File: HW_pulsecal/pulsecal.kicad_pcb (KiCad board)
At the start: 2 copper layers, 98 x 98 mm, 92 parts, among them J1 BNC_CONN, J2 USB_C_Receptacle_USB2.0, J3 Conn_01x02, J4 Conn_01x04, Q1 AO3401A, Q3 FDG6301N, SW1 SW_Push, SW2 SW_Push, SW3 SW_Push, SW4 SW_Push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

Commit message: update
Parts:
- added REF**: KiCad-Logo2_5mm_SilkScreen, Symbol:KiCad-Logo2_5mm_SilkScreen, F.Cu at (46.2, 99.7)
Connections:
- U5 pad 20: unconnected-(U5-PB1-Pad20) -> DISP_F
- U5 pad 21: unconnected-(U5-PB2-Pad21) -> DISP_D
- U5 pad 22: unconnected-(U5-PB10-Pad22) -> DISP_DIG2
- U5 pad 23: unconnected-(U5-PB11-Pad23) -> DISP_C
- U5 pad 24: unconnected-(U5-PB12-Pad24) -> DISP_J
- U5 pad 26: unconnected-(U5-PB14-Pad26) -> DISP_H
- U5 pad 27: unconnected-(U5-PB15-Pad27) -> DISP_DIG1
- U5 pad 29: unconnected-(U5-PA9/NC-Pad29) -> DISP_DP
- U5 pad 30: unconnected-(U5-PC6-Pad30) -> DISP_A
- U5 pad 31: unconnected-(U5-PC7-Pad31) -> DISP_E
- U5 pad 32: unconnected-(U5-PA10/NC-Pad32) -> DISP_DIG3
- U5 pad 33: unconnected-(U5-PA11/PA9-Pad33) -> DISP_N
- U5 pad 34: unconnected-(U5-PA12/PA10-Pad34) -> DISP_B
- U5 pad 37: unconnected-(U5-PA15-Pad37) -> DISP_M
- U5 pad 38: unconnected-(U5-PD0-Pad38) -> DISP_DIG4
- U5 pad 39: unconnected-(U5-PD1-Pad39) -> DISP_L
- U5 pad 40: unconnected-(U5-PD2-Pad40) -> DISP_DIG5
- U5 pad 41: unconnected-(U5-PD3-Pad41) -> DISP_G2
- U5 pad 42: unconnected-(U5-PB3-Pad42) -> DISP_K
- U5 pad 43: unconnected-(U5-PB4-Pad43) -> DISP_G1
- U5 pad 44: unconnected-(U5-PB5-Pad44) -> DISP_DIG6
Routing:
- net DISP_D: track 0.00 -> 28.2 mm, vias 0 -> 2
- net DISP_F: track 0.00 -> 28.2 mm, vias 0 -> 2
- net DISP_DIG6: track 5.29 -> 33.3 mm
- net DISP_G1: track 0.00 -> 27.6 mm
- net DISP_DIG2: track 5.28 -> 32.9 mm, vias 0 -> 2
- net DISP_C: track 0.00 -> 27.6 mm, vias 0 -> 2
- net DISP_DP: track 0.00 -> 27.3 mm
- net DISP_J: track 0.00 -> 27.3 mm, vias 0 -> 2
- net DISP_B: track 0.00 -> 27.2 mm
- net DISP_N: track 0.00 -> 27.1 mm
- net unconnected-(U5-PA9/NC-Pad29): track 27.0 -> 0.00 mm
- net DISP_A: track 0.00 -> 27.0 mm
- net DISP_K: track 0.00 -> 27.0 mm
- net DISP_E: track 0.00 -> 26.6 mm
- net DISP_DIG3: track 5.33 -> 31.8 mm
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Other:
- board text added: "!"
- board text added: "ADD"
- board text added: "BAT"
- board text added: "HIGH VOLTAGE"
- board text added: "Hz/KHz/MHz"
- board text added: "MOVE"
- board text added: "OUTPUT"
- board text added: "Pulse Generator for Scaler/Ratemeter"
- board text added: "SUB"
- board text added: "USB"
- board text added: "V/KV"
- board text added: "V1.0"
- board text added: "by Analog Dragon"
- board text added: "nS/uS"

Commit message: update
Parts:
- R1, R15: value 1k -> 1K
- R11: value 2.2k -> 2.2K
- R12, R13: value 1G -> 500M
- R14, R5, R6, R7: value 10k -> 10K
- R16, R17, R18, R19, R20, R21, R22, R23, R24, R25, R26, R27, R28, R29, R30: value 10K -> 330R
- R34, R35: value 5K1 -> 5.1K
- SW1, SW2, SW3, SW4, SW5, SW6, SW7: value SW_Push -> 6*6*5 100g; footprint Button_Switch_SMD:SW_SPST_PTS647_Sx38 -> Button_Switch_SMD:SW_SPST_PTS645
- U4: value TX4310 -> TX4310B
- moved SW4 1.15 mm to (121.9, 111.0)
- moved SW1 0.40 mm to (108.4, 107.0)
- moved SW2 0.40 mm to (108.4, 115.0)
- moved SW3 0.40 mm to (108.4, 123.0)
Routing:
- net GND: track 134.8 -> 150.7 mm, vias 381 -> 379
- net key_add: track 72.2 -> 58.9 mm
- net key_freq: track 69.7 -> 71.9 mm
- net key_pulse: track 72.9 -> 70.7 mm
- net key_volt: track 78.2 -> 80.3 mm
- net key_output: track 82.1 -> 84.2 mm
- net key_move: track 60.2 -> 62.3 mm
- net Net-(J1-In): track 15.5 -> 17.2 mm
- net key_sub: track 68.8 -> 69.9 mm
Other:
- board text added: "V1.1"
- board text removed: "V1.0"

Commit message: update
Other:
- board text added: "mV/V"
- board text removed: "V/KV"
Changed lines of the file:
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@@
 		)
 	)
-	(gr_text "V/KV"
+	(gr_text "mV/V"
 		(at 106.8 127.5 0)
 		(layer "F.SilkS")

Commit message: update
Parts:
- added G***: LOGO, LOGO, F.Cu at (61.9, 98.5)
- moved REF** 0.61 mm to (46.1, 99.1)
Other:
- board text added: "2~5V"

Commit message: Update pulsecal.kicad_pcb
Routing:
- net Net-(J1-In): track 17.2 -> 15.7 mm
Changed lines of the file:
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@@
 			(layer "F.SilkS")
 		)
+		(fp_line
+			(start -6 -3.2)
+			(end 6 -3.2)
+			(stroke
+				(width 0.05)
+				(type default)
+			)
+			(layer "Edge.Cuts")
+		)
+		(fp_line
+			(start 6 -1.2)
+			(end -6 -1.2)
+			(stroke
+				(width 0.05)
+				(type default)
+			)
+			(layer "Edge.Cuts")
+		)
+		(fp_arc
+			(start -6 -1.2)
+			(mid -7 -2.2)
+			(end -6 -3.2)
+			(stroke
+				(width 0.05)
+				(type default)
+			)
+			(layer "Edge.Cuts")
+		)
+		(fp_arc
+			(start 6 -3.2)
+			(mid 7 -2.2)
+			(end 6 -1.2)
+			(stroke
+				(width 0.05)
+				(type default)
+			)
+			(layer "Edge.Cuts")
+		)
 		(fp_text user "${REFERENCE}"
 			(at 0 -2.5 0)
@@
 		)
 		(pad "1" smd roundrect
-			(at 0 0.75)
-			(size 2 6)
+			(at 0 2.25)
+			(size 2 3)
 			(layers "F.Cu" "F.Paste" "F.Mask")
 			(roundrect_rratio 0.0625)
@@
 	)
 	(segment
-		(start 51.31 43.25)
-		(end 51.31 48.39)
+		(start 51.3 48.4)
+		(end 55.5375 48.4)
 		(width 1)
 		(layer "F.Cu")
@@
 	)
 	(segment
-		(start 51.3 48.4)
-		(end 55.5375 48.4)
+		(start 51.31 44.75)
+		(end 51.31 48.39)
 		(width 1)
 		(layer "F.Cu")

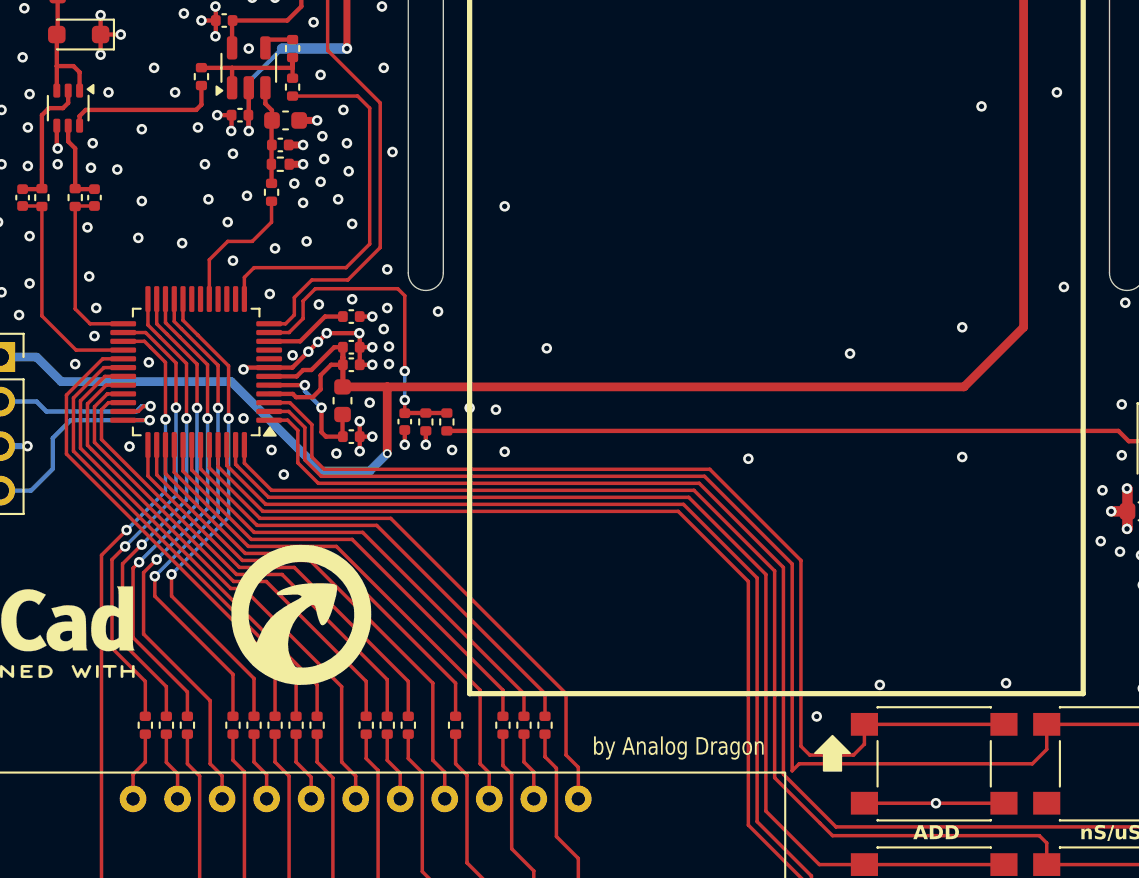
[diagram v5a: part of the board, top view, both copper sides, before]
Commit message: 更新
增加了一个电阻，可以极大的减少低压输出的振铃
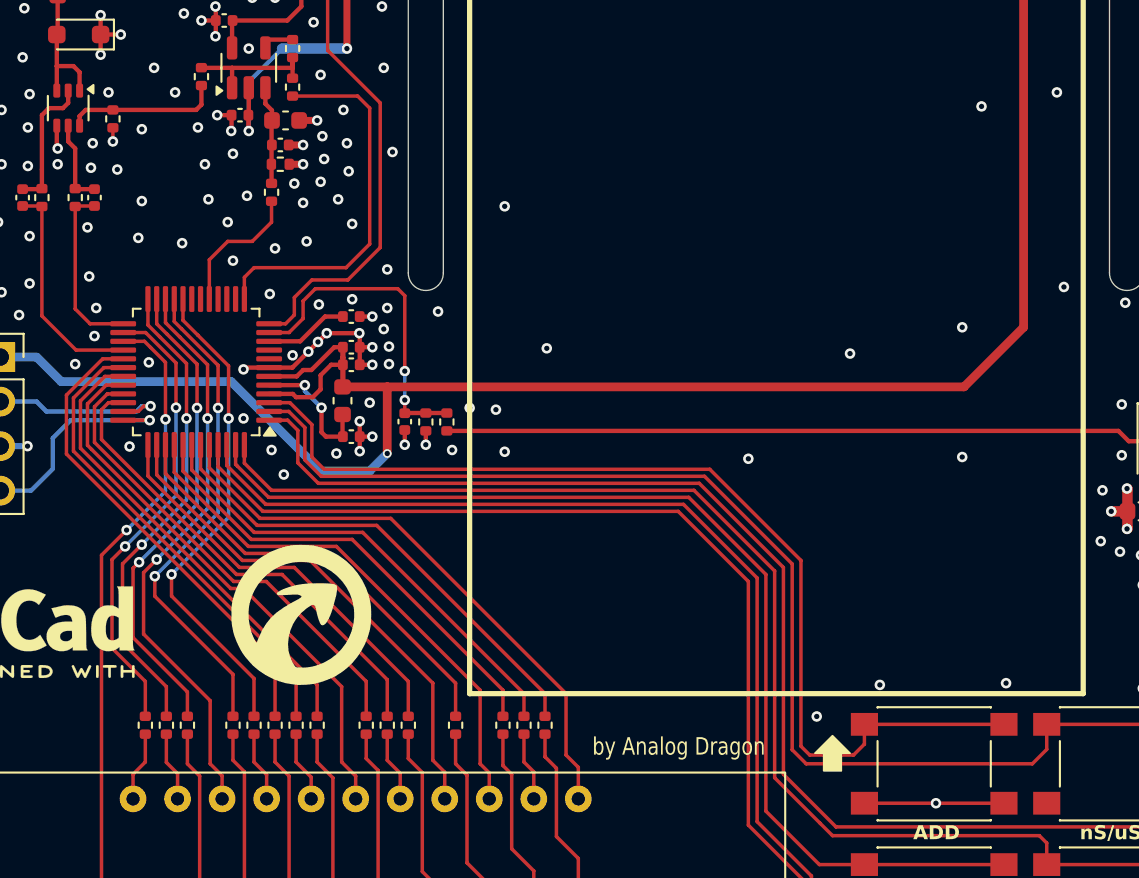
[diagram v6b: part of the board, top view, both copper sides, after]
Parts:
- added R37: 100R, Resistor_SMD:R_0402_1005Metric, F.Cu at (51.1, 70.2)
- R15: value 1K -> NC
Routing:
- net key_pulse: track 70.7 -> 69.7 mm
- net GND: track 150.7 -> 151.5 mm, vias 379 -> 380

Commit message: update
范围改成2mV-999mV
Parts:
- R15: value NC -> 1K
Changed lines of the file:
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@@
 			)
 		)
-		(property "Value" "NC"
+		(property "Value" "1K"
 			(at 0 1.17 0)
 			(layer "F.Fab")

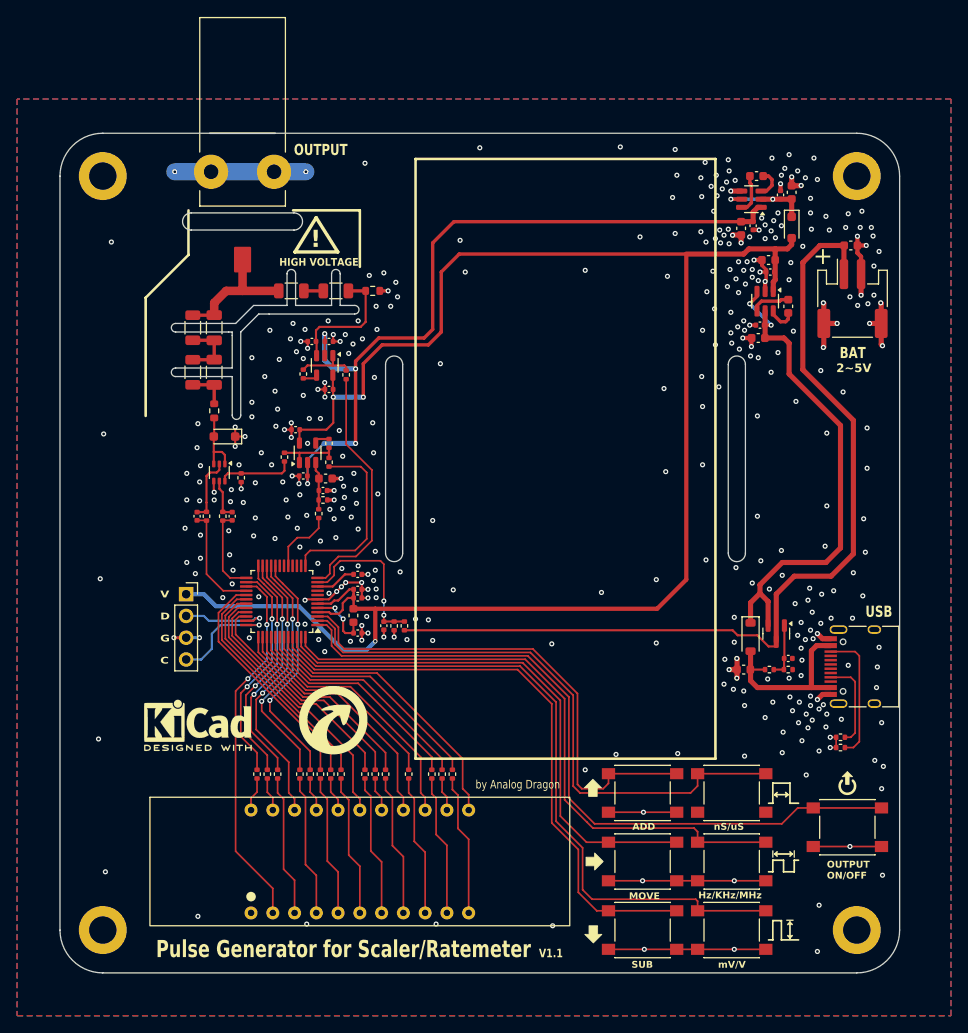
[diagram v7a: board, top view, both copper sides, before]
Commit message: update v1.2
改连接器，改贴片器件为直插器件
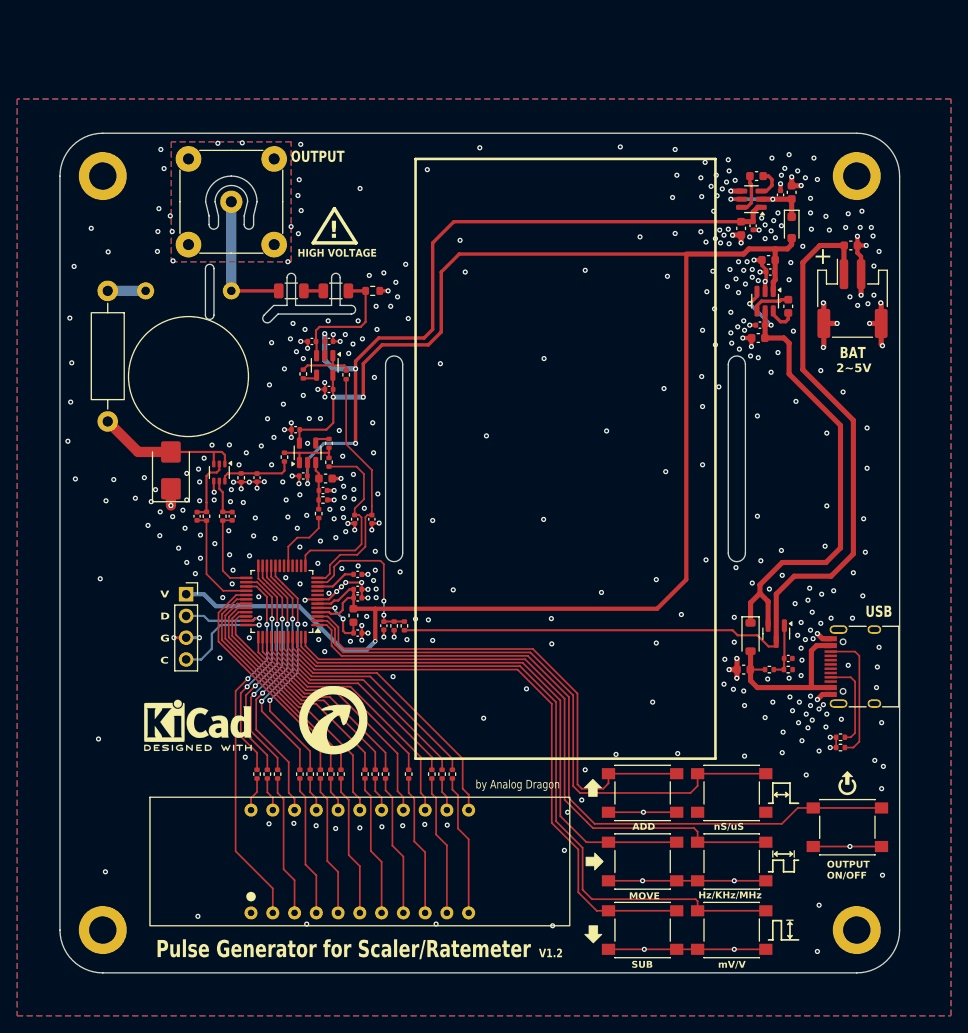
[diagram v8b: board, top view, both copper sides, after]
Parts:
- removed R12, R13: 500M, Resistor_SMD:R_1206_3216Metric
- added C30: 103/50V, Capacitor_SMD:C_0402_1005Metric, F.Cu at (66.4, 75.0)
- added C31: 103/50V, Capacitor_SMD:C_0402_1005Metric, F.Cu at (64.4, 75.0)
- C1: value 10nF/2kV -> 10nF/4kV; footprint Capacitor_SMD:C_1206_3216Metric -> Capacitor_THT:C_Rect_L13.5mm_W4.0mm_P10.00mm_FKS3_FKP3_MKS4
- C2: value 10nF/2kV -> NC; footprint Capacitor_SMD:C_1206_3216Metric -> Capacitor_SMD:C_0402_1005Metric
- D1: value TVS_3V3 -> SMBJ3.3CA; footprint Diode_SMD:D_SOD-323_HandSoldering -> Diode_SMD:D_SMB
- J1: footprint NewLib:BNC_3pin -> Connector_Coaxial:BNC_TEConnectivity_1478204_Vertical
- R1: value 1K -> 100R; footprint Resistor_SMD:R_0603_1608Metric -> Resistor_THT:R_Axial_DIN0411_L9.9mm_D3.6mm_P15.24mm_Horizontal
- R14, R7: value 10K -> 100R
- moved R1 18.7 mm to (35.6, 48.4)
- moved C2 13.3 mm to (53.0, 70.2)
- moved D1 7.39 mm to (43.0, 69.3), turned to 90 degrees
- moved C1 4.74 mm to (50.0, 48.4), turned to 180 degrees
- moved J1 4.69 mm to (50.0, 38.0)
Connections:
- C2 pad 1: Net-(C1-Pad2) -> Net-(Q3A-D)
- C2 pad 2: Net-(C2-Pad2) -> GND
- R1 pad 1: Net-(C2-Pad2) -> Net-(C1-Pad2)
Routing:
- net Net-(D1-A2): track 7.89 -> 17.7 mm
- net GND: track 151.5 -> 142.3 mm, vias 380 -> 449
- net Net-(C2-Pad2): track 4.71 -> 0.00 mm
- net Net-(C1-Pad2): track 7.26 -> 4.42 mm
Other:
- outline, holes or cut-outs redrawn
- board text added: "V1.2"
- board text removed: "V1.1"
